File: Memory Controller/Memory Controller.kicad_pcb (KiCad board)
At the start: 4 copper layers, 39 parts, among them J1 Conn_01x05, J2 Conn_01x02, J3 Conn_02x15_Odd_Even, J4 Conn_02x08_Top_Bottom, J5 Conn_02x15_Odd_Even, J6 Conn_01x01, U1 74AHC1G32, U10 SN74AHCT16374DGGR, U11 74AHC1G08, U12 SST39SF010, U13 SST39SF010, U14 71016S12PHG8, U2 74AHC1G04, U3 74AHC1G32, U4 74AHC1G32, U5 74AHC1G32, U6 74AHC1G04, U7 74AHC1G32, U8 74AHC1G32, U9 74AHC1G32

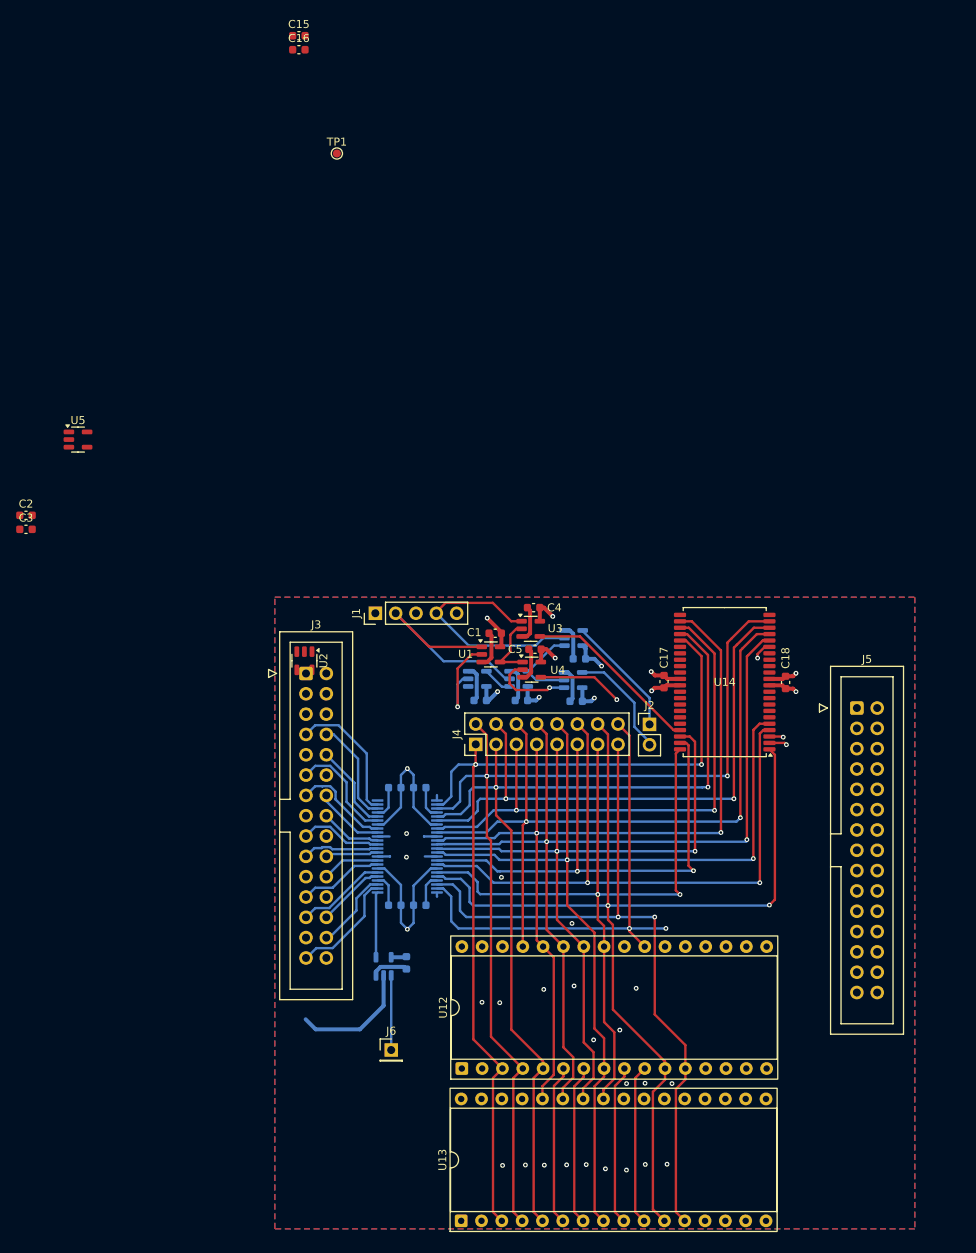
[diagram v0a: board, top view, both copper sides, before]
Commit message: Memory Controller first draft
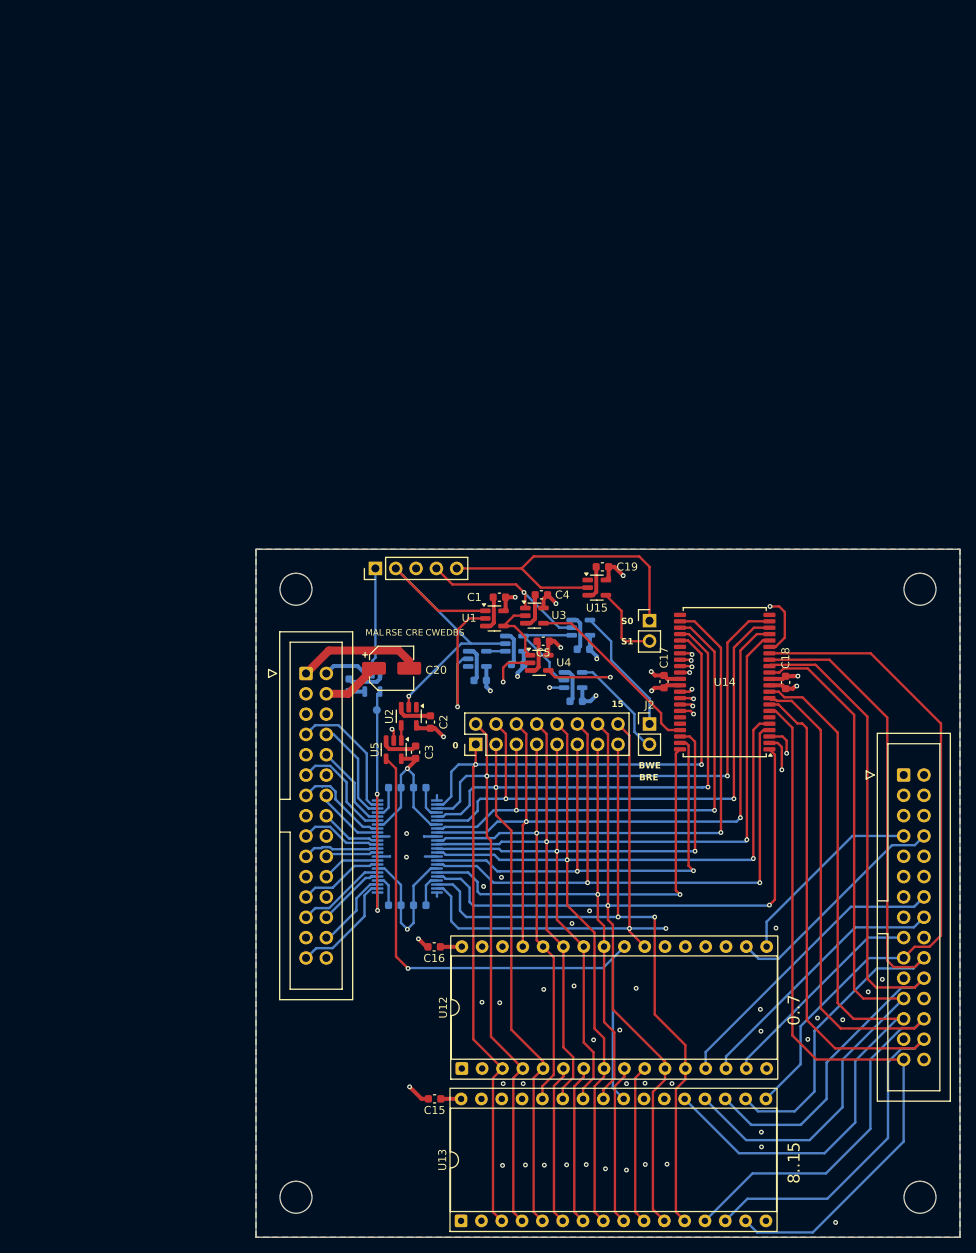
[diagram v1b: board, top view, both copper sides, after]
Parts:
- added C19: C, Capacitor_SMD:C_0603_1608Metric, F.Cu at (66.3, 10.2)
- added C20: C, Capacitor_SMD:CP_Elec_5x5.3, F.Cu at (40.0, 22.9)
- added H1: MountingHole, MountingHole:MountingHole_4mm, F.Cu at (28.0, 13.0)
- added H2: MountingHole, MountingHole:MountingHole_4mm, F.Cu at (28.0, 89.0)
- added H3: MountingHole, MountingHole:MountingHole_4mm, F.Cu at (106.0, 13.0)
- added H4: MountingHole, MountingHole:MountingHole_4mm, F.Cu at (106.0, 89.0)
- added U15: 74AHC1G04, Package_TO_SOT_SMD:SOT-23-5, F.Cu at (65.6, 12.8)
- J6: value Conn_01x01 -> Conn_01x02; footprint Connector_PinHeader_2.54mm:PinHeader_1x01_P2.54mm_Vertical -> Connector_PinHeader_2.54mm:PinHeader_1x02_P2.54mm_Vertical
- TP1: moved to B.Cu
- moved C15 134.0 mm to (45.3, 76.7), turned to 180 degrees
- moved C16 113.4 mm to (45.3, 57.7), turned to 180 degrees
- moved TP1 69.7 mm to (38.1, 28.1)
- moved J6 62.6 mm to (72.2, 16.9)
- moved C2 56.8 mm to (44.8, 29.6), turned to 90 degrees
- moved C3 56.1 mm to (43.0, 33.4), turned to 90 degrees
- moved U5 55.3 mm to (40.2, 33.0), turned to -90 degrees
- moved U11 35.5 mm to (37.5, 24.6), turned to -90 degrees
- moved C14 35.4 mm to (34.6, 25.0), turned to 90 degrees
- moved U2 14.8 mm to (42.1, 28.9)
- moved J5 10.2 mm to (104.0, 36.2)
- moved J1 5.60 mm to (37.9, 10.4)
- moved C1 4.53 mm to (53.4, 14.0)
- moved C6 4.52 mm to (55.7, 22.4)
- moved U1 4.52 mm to (52.8, 16.6)
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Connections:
- J1 pad 1: /GRE -> /MAL
- J5 pad 1: /bus_conn1/GND -> GND
- J5 pad 12: /bus_conn1/GND -> GND
- J5 pad 15: /bus_conn1/GND -> GND
- J5 pad 18: /bus_conn1/GND -> GND
- J5 pad 21: /bus_conn1/GND -> GND
- J5 pad 24: /bus_conn1/GND -> GND
- J5 pad 27: /bus_conn1/GND -> GND
- J5 pad 3: /bus_conn1/GND -> GND
- J5 pad 30: /bus_conn1/GND -> GND
- J5 pad 5: /bus_conn1/GND -> GND
- J5 pad 6: /bus_conn1/GND -> GND
- J5 pad 9: /bus_conn1/GND -> GND
- J6 pad 1: /MAL -> /DBS
- U5 pad 1: /CRE -> Net-(U2-Pad4)
- U5 pad 2: Net-(U2-Pad4) -> /CRE
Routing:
- net /ROM/DATA13: track 0.00 -> 100.2 mm
- net /ROM/DATA14: track 0.00 -> 98.8 mm
- net /ROM/DATA12: track 0.00 -> 95.2 mm
- net /ROM/DATA15: track 0.00 -> 92.7 mm
- net /ROM/DATA10: track 0.00 -> 92.2 mm
- net /ROM/DATA11: track 0.00 -> 92.0 mm
- net /ROM/DATA9: track 0.00 -> 88.9 mm
- net /ROM/DATA5: track 0.00 -> 86.3 mm, vias 0 -> 1
- net /ROM/DATA8: track 0.00 -> 84.7 mm
- net /ROM/DATA6: track 0.00 -> 84.2 mm, vias 0 -> 1
- net /ROM/DATA2: track 0.00 -> 80.1 mm, vias 0 -> 1
- net /ROM/DATA4: track 0.00 -> 79.7 mm, vias 0 -> 1
- net /ROM/DATA1: track 0.00 -> 79.1 mm, vias 0 -> 1
- net /ROM/DATA7: track 0.00 -> 76.0 mm, vias 0 -> 1
- net /ROM_RE: track 0.00 -> 73.7 mm, vias 0 -> 1
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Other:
- board outline added: 88 x 86 mm
- board text added: "0"
- board text added: "0..7"
- board text added: "15"
- board text added: "8..15"
- board text added: "BRE"
- board text added: "BWE"
- board text added: "CRE"
- board text added: "CWE"
- board text added: "DBS"
- board text added: "MAL"
- board text added: "RSE"
- board text added: "S0"
- board text added: "S1"

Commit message: Memory Controller fabrication checks complete
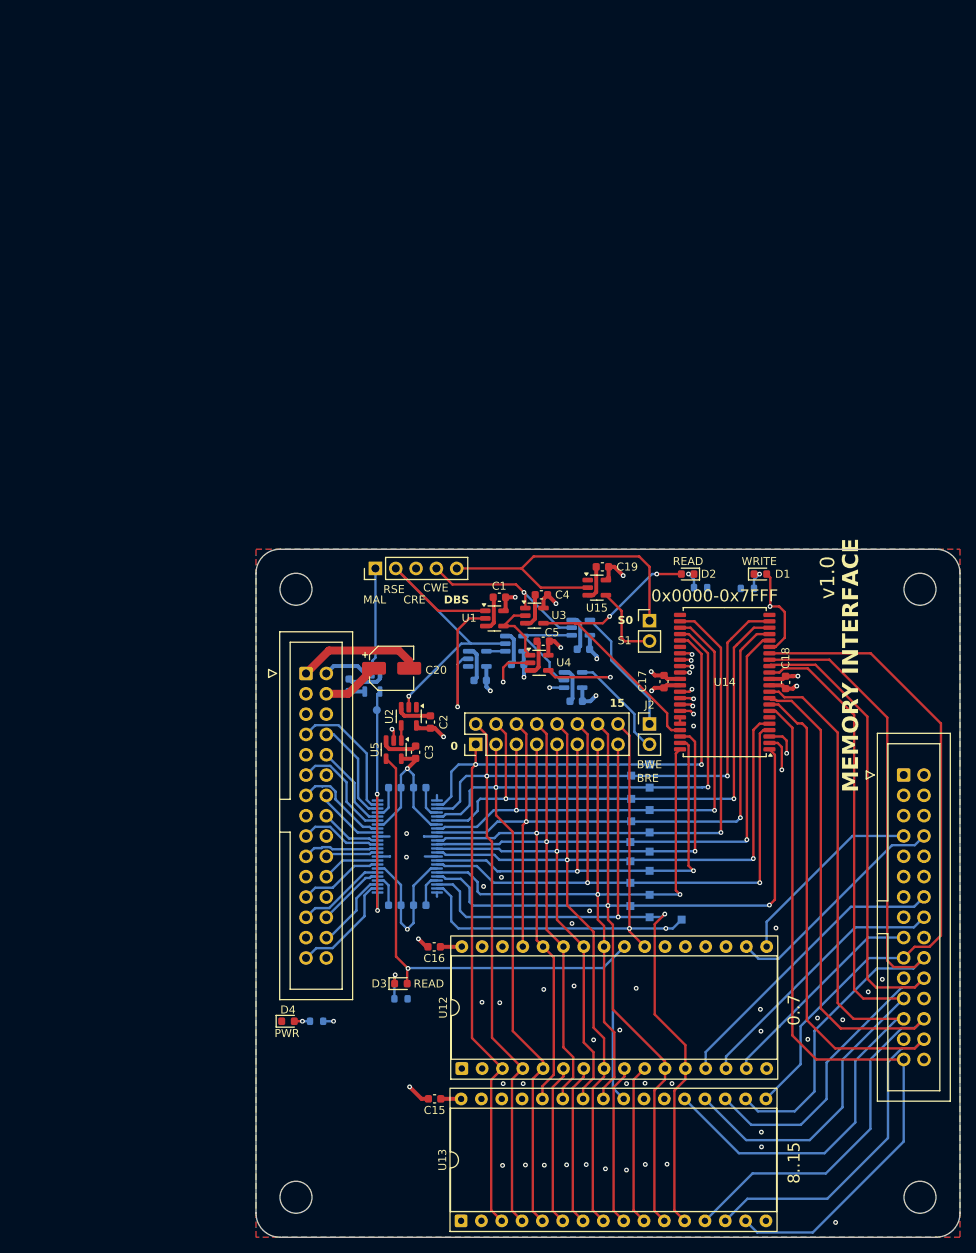
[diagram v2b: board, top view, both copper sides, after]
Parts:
- added D1: LED, LED_SMD:LED_0603_1608Metric, F.Cu at (86.0, 11.1)
- added D2: LED, LED_SMD:LED_0603_1608Metric, F.Cu at (77.0, 11.1)
- added D3: LED, LED_SMD:LED_0603_1608Metric, F.Cu at (41.1, 62.3)
- added D4: LED, LED_SMD:LED_0603_1608Metric, F.Cu at (27.0, 67.0)
- added R1: R, Resistor_SMD:R_0603_1608Metric, B.Cu at (84.4, 12.9)
- added R2: R, Resistor_SMD:R_0603_1608Metric, B.Cu at (78.6, 12.8)
- added R3: R, Resistor_SMD:R_0603_1608Metric, B.Cu at (41.1, 64.2)
- added R4: R, Resistor_SMD:R_0603_1608Metric, B.Cu at (30.6, 67.0)
- added TP10: TestPoint_Small, TestPoint:TestPoint_Pad_1.0x1.0mm, B.Cu at (72.2, 45.8)
- added TP11: TestPoint_Small, TestPoint:TestPoint_Pad_1.0x1.0mm, B.Cu at (69.8, 47.0)
- added TP12: TestPoint_Small, TestPoint:TestPoint_Pad_1.0x1.0mm, B.Cu at (72.2, 48.2)
- added TP13: TestPoint_Small, TestPoint:TestPoint_Pad_1.0x1.0mm, B.Cu at (69.8, 49.7)
- added TP14: TestPoint_Small, TestPoint:TestPoint_Pad_1.0x1.0mm, B.Cu at (72.2, 51.2)
- added TP15: TestPoint_Small, TestPoint:TestPoint_Pad_1.0x1.0mm, B.Cu at (69.8, 52.6)
- added TP16: TestPoint_Small, TestPoint:TestPoint_Pad_1.0x1.0mm, B.Cu at (72.2, 54.0)
- added TP17: TestPoint_Small, TestPoint:TestPoint_Pad_1.0x1.0mm, B.Cu at (76.2, 54.3)
- added TP2: TestPoint_Small, TestPoint:TestPoint_Pad_1.0x1.0mm, B.Cu at (72.2, 34.9)
- added TP3: TestPoint_Small, TestPoint:TestPoint_Pad_1.0x1.0mm, B.Cu at (69.9, 36.3)
- added TP4: TestPoint_Small, TestPoint:TestPoint_Pad_1.0x1.0mm, B.Cu at (72.2, 37.8)
- added TP5: TestPoint_Small, TestPoint:TestPoint_Pad_1.0x1.0mm, B.Cu at (69.9, 39.2)
- added TP6: TestPoint_Small, TestPoint:TestPoint_Pad_1.0x1.0mm, B.Cu at (72.2, 40.6)
- added TP7: TestPoint_Small, TestPoint:TestPoint_Pad_1.0x1.0mm, B.Cu at (69.9, 42.0)
- added TP8: TestPoint_Small, TestPoint:TestPoint_Pad_1.0x1.0mm, B.Cu at (72.2, 43.4)
- added TP9: TestPoint_Small, TestPoint:TestPoint_Pad_1.0x1.0mm, B.Cu at (69.8, 44.6)
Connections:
- net /RAM_RE renamed /~{RAM_RE}
- net /RAM_WE renamed /~{RAM_WE}
- net /ROM_RE renamed /~{ROM_RE}
- U12 pad 10: /word_conn/IN2 -> /word_conn/IN11
- U12 pad 11: /word_conn/IN1 -> /word_conn/IN13
- U12 pad 12: /word_conn/IN0 -> /word_conn/IN14
- U12 pad 13: /ROM/DATA0 -> /ROM/DATA5
- U12 pad 14: /ROM/DATA1 -> /ROM/DATA6
- U12 pad 15: /ROM/DATA2 -> /ROM/DATA7
- U12 pad 17: /ROM/DATA3 -> /ROM/DATA0
- U12 pad 18: /ROM/DATA4 -> /ROM/DATA1
- U12 pad 19: /ROM/DATA5 -> /ROM/DATA2
- U12 pad 20: /ROM/DATA6 -> /ROM/DATA3
- U12 pad 21: /ROM/DATA7 -> /ROM/DATA4
- U12 pad 23: /word_conn/IN10 -> /word_conn/IN15
- U12 pad 25: /word_conn/IN11 -> /word_conn/IN12
- U12 pad 26: /word_conn/IN9 -> /word_conn/IN8
- U12 pad 27: /word_conn/IN8 -> /word_conn/IN7
- U12 pad 28: /word_conn/IN13 -> /word_conn/IN6
- U12 pad 29: /word_conn/IN14 -> /word_conn/IN5
- U12 pad 3: /word_conn/IN15 -> /word_conn/IN0
- U12 pad 4: /word_conn/IN12 -> /word_conn/IN1
- U12 pad 5: /word_conn/IN7 -> /word_conn/IN2
- U12 pad 6: /word_conn/IN6 -> /word_conn/IN3
- U12 pad 7: /word_conn/IN5 -> /word_conn/IN4
- U12 pad 8: /word_conn/IN4 -> /word_conn/IN9
- U12 pad 9: /word_conn/IN3 -> /word_conn/IN10
- U13 pad 10: /word_conn/IN2 -> /word_conn/IN11
- U13 pad 11: /word_conn/IN1 -> /word_conn/IN13
- U13 pad 12: /word_conn/IN0 -> /word_conn/IN14
- U13 pad 13: /ROM/DATA8 -> /ROM/DATA13
- U13 pad 14: /ROM/DATA9 -> /ROM/DATA14
- U13 pad 15: /ROM/DATA10 -> /ROM/DATA15
- U13 pad 17: /ROM/DATA11 -> /ROM/DATA8
- U13 pad 18: /ROM/DATA12 -> /ROM/DATA9
- U13 pad 19: /ROM/DATA13 -> /ROM/DATA10
- U13 pad 20: /ROM/DATA14 -> /ROM/DATA11
- U13 pad 21: /ROM/DATA15 -> /ROM/DATA12
- U13 pad 23: /word_conn/IN10 -> /word_conn/IN15
- U13 pad 25: /word_conn/IN11 -> /word_conn/IN12
- U13 pad 26: /word_conn/IN9 -> /word_conn/IN8
- U13 pad 27: /word_conn/IN8 -> /word_conn/IN7
- U13 pad 28: /word_conn/IN13 -> /word_conn/IN6
- U13 pad 29: /word_conn/IN14 -> /word_conn/IN5
- U13 pad 3: /word_conn/IN15 -> /word_conn/IN0
- U13 pad 4: /word_conn/IN12 -> /word_conn/IN1
- U13 pad 5: /word_conn/IN7 -> /word_conn/IN2
- U13 pad 6: /word_conn/IN6 -> /word_conn/IN3
- U13 pad 7: /word_conn/IN5 -> /word_conn/IN4
- U13 pad 8: /word_conn/IN4 -> /word_conn/IN9
- U13 pad 9: /word_conn/IN3 -> /word_conn/IN10
- U14 pad 1: /word_conn/IN0 -> /word_conn/IN13
- U14 pad 10: /ROM/DATA6 -> /ROM/DATA12
- U14 pad 13: /ROM/DATA8 -> /ROM/DATA11
- U14 pad 15: /ROM/DATA12 -> /ROM/DATA9
- U14 pad 16: /ROM/DATA14 -> /ROM/DATA8
- U14 pad 18: /word_conn/IN15 -> /word_conn/IN7
- U14 pad 19: /word_conn/IN13 -> /word_conn/IN5
- U14 pad 2: /word_conn/IN2 -> /word_conn/IN15
- U14 pad 20: /word_conn/IN11 -> /word_conn/IN3
- U14 pad 21: /word_conn/IN9 -> /word_conn/IN1
- U14 pad 24: /word_conn/IN8 -> /word_conn/IN6
- U14 pad 25: /word_conn/IN10 -> /word_conn/IN4
- U14 pad 26: /word_conn/IN12 -> /word_conn/IN2
- U14 pad 27: /word_conn/IN14 -> /word_conn/IN0
- U14 pad 29: /ROM/DATA15 -> /ROM/DATA0
- U14 pad 3: /word_conn/IN4 -> /word_conn/IN14
- U14 pad 30: /ROM/DATA13 -> /ROM/DATA1
- U14 pad 31: /ROM/DATA11 -> /ROM/DATA2
- U14 pad 32: /ROM/DATA9 -> /ROM/DATA3
- U14 pad 35: /ROM/DATA7 -> /ROM/DATA4
- U14 pad 37: /ROM/DATA3 -> /ROM/DATA6
- U14 pad 38: /ROM/DATA1 -> /ROM/DATA7
- U14 pad 4: /word_conn/IN6 -> /word_conn/IN11
- U14 pad 42: /word_conn/IN5 -> /word_conn/IN8
- U14 pad 43: /word_conn/IN3 -> /word_conn/IN10
- U14 pad 44: /word_conn/IN1 -> /word_conn/IN12
- U14 pad 5: /word_conn/IN7 -> /word_conn/IN9
- U14 pad 7: /ROM/DATA0 -> /ROM/DATA15
- U14 pad 8: /ROM/DATA2 -> /ROM/DATA14
- U14 pad 9: /ROM/DATA4 -> /ROM/DATA13
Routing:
- net /~{RAM_RE}: track 23.3 -> 39.4 mm, vias 0 -> 2
- net Net-(D3-K): track 0.00 -> 4.17 mm, vias 0 -> 1
- net /~{RAM_WE}: track 40.0 -> 43.6 mm
- net /CRE: track 54.6 -> 51.4 mm
- net Net-(D1-K): track 0.00 -> 2.80 mm, vias 0 -> 1
- net Net-(D2-K): track 0.00 -> 2.68 mm, vias 0 -> 1
- net /word_conn/IN15: track 158.8 -> 161.2 mm
- net Net-(D4-A): track 0.00 -> 1.96 mm, vias 0 -> 1
- net /~{ROM_RE}: track 73.7 -> 75.6 mm
- net /word_conn/IN14: track 130.1 -> 131.7 mm
- net +5V: track 97.7 -> 98.7 mm, vias 13 -> 14
- net GND: track 101.7 -> 102.5 mm, vias 42 -> 43
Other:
- outline, holes or cut-outs redrawn
- board text added: "0x0000-0x7FFF"
- board text added: "MEMORY ADDRESS REGISTER"
- board text added: "MEMORY INTERFACE"
- board text added: "PWR"
- board text added: "READ"
- board text added: "WRITE"
- board text added: "v1.0"
